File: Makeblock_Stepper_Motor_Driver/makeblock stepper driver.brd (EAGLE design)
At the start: 100 x 80 mm, 7 parts, among them IC1 A4988SETTR-T

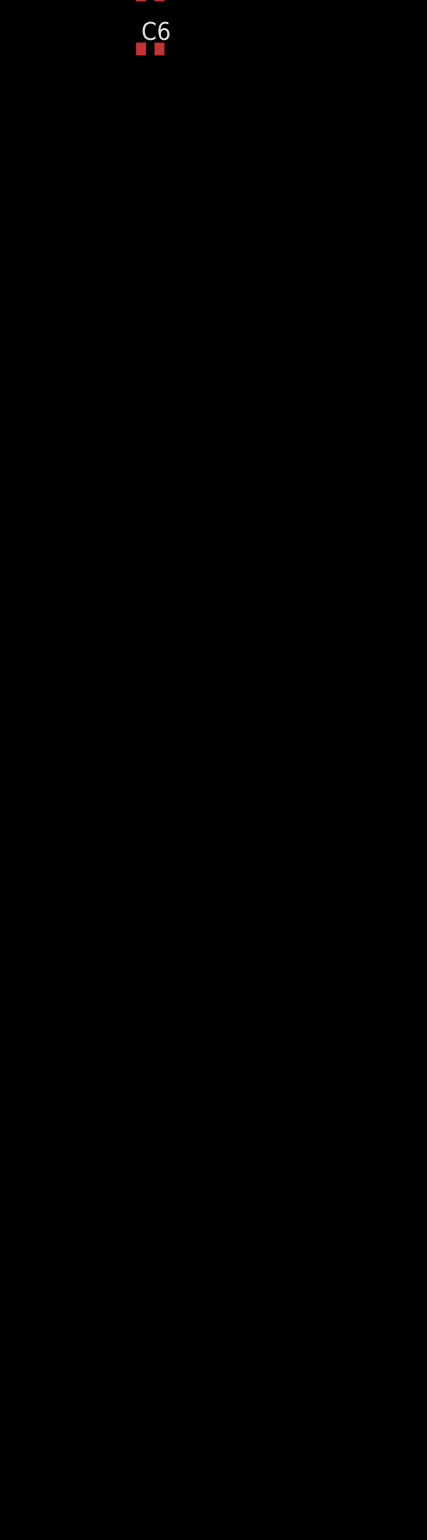
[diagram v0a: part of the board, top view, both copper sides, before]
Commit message: Added parts to the schematic
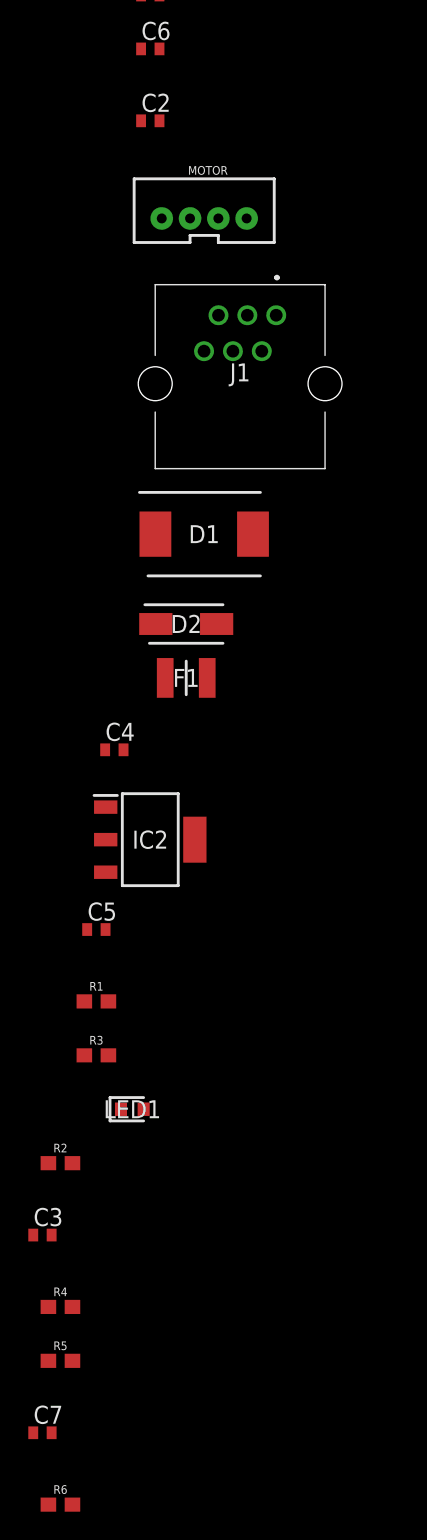
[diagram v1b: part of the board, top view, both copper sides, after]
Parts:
- added C2, C3, C4, C5, C7: 0.1uF, resistor:C0402
- added D1: SS34, SamacSys_Parts:DIOM8059X256N
- added D2: SS14, SamacSys_Parts:DIOM5227X270N
- added F1: 0ZCH0075AF2E, SamacSys_Parts:FUSC3226X75N
- added IC2: LD1117ASTR, SamacSys_Parts:SOT230P700X180-4N
- added J1: E5566-Q0LK22-L, SamacSys_Parts:E5566Q0LK22L
- added LED1: SML-D12U1WT86, SamacSys_Parts:LEDC1608X65N
- added MOTOR: (no value), SparkFun-Connectors:JST-4-PTH-VERT
- added R1, R4, R5, R6: 10M, SparkFun-Resistors:0603
- added R2: 100k, SparkFun-Resistors:0603
- added R3: 2.2k, SparkFun-Resistors:0603
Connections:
- removed net VCC: RN1.1, S1.1, S1.2, S1.3
- new net 1A: IC1.24, MOTOR.3
- new net 1B: IC1.21, MOTOR.4
- new net 2A: IC1.26, MOTOR.2
- new net 2B: IC1.1, MOTOR.1
- new net DIR: J1.5
- new net N$10: LED1.2, R3.1
- new net N$11: C5.2, IC2.2, IC2.4, R3.2
- new net N$12: IC1.2, R2.2
- new net N$13: C3.2, IC1.6
- new net N$14: IC1.27, R4.1
- new net N$15: IC1.23, R5.1
- new net N$16: IC1.19
- new net N$3: J1.1
- new net N$4: C2.2, IC1.28
- new net N$5: D1.1, F1.1
- new net N$6: C4.2, IC2.3
- new net N$9: J1.2
- new net PGND: C2.1, C7.1, IC1.18, IC1.29, IC1.3, R1.1, R5.2
- new net STEP: J1.6
- new net V-M: D1.2, D2.2, J1.3
- new net VM: C3.1, C7.2, F1.2, IC1.22
- net 5V: now also R6.2, RN1.1, S1.1, S1.2, S1.3
- net GND: now also C4.1, C5.1, D2.1, IC2.1, J1.4, LED1.1, R1.2, R2.1

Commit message: Finshed the schematic and the layout
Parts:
- added C10: 0.1u, resistor:C0402
- added P2: (no value), SparkFun-Connectors:1X04
- added P3: (no value), SparkFun-Connectors:1X03_LOCK
- added R7: 0.2R, SparkFun-Resistors:0603
- C1: value (none) -> 0.1uF
- C3: value 0.1uF -> 22uF; device resistor:C0402 -> rcl:C025-024X044
- R1: value 10M -> 0.2R
- R2: value 100k -> 0.2R
- R4: value 10M -> 27k
- R5: value 10M -> 100k
- R6: value 10M -> PVG3A203C01R00; device SparkFun-Resistors:0603 -> SamacSys_Parts:PVG3A203C01R00
- moved R6 148.2 mm to (13.0, 19.8)
- moved C7 138.6 mm to (19.9, 11.4)
- moved R5 130.7 mm to (19.7, 8.48)
- moved R4 123.7 mm to (2.71, 11.3)
- moved C3 118.2 mm to (20.5, 2.50)
- moved R2 111.5 mm to (8.21, 6.51)
- moved R3 110.8 mm to (25.2, 6.10)
- moved LED1 109.5 mm to (25.3, 2.29)
- moved R1 102.8 mm to (15.2, 6.32)
- moved C5 99.7 mm to (2.75, 13.5)
- moved IC2 99.6 mm to (5.08, 20.3)
- moved D1 91.5 mm to (24.6, 25.4), turned to 90 degrees
- moved J1 91.3 mm to (11.5, 44.5), turned to 180 degrees
- moved D2 90.2 mm to (25.4, 16.1), turned to 90 degrees
- moved C4 88.9 mm to (2.54, 15.2), turned to 180 degrees
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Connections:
- removed net N$12: IC1.2, R2.2
- removed net N$4: C2.2, IC1.28
- removed net ROSC: IC1.13, RN1.2
- new net EN: IC1.2, P3.1, R5.2
- new net N$17: IC1.17, R6.2
- net !RESET: now also C10.1, P3.2; no longer C1.1
- net !SLEEP: now also P3.3
- net 5V: now also R4.2; no longer R6.2
- net DIR: now also IC1.19, P2.2
- net GND: now also C10.2, P2.3, R5.1, R6.3, R7.2, RN1.2; no longer C1.2, C9.1, D2.1, R1.2, R2.1, RN1.7
- net N$13: now also C7.2; no longer C3.2
- net N$14: now also R1.1; no longer R4.1
- net N$15: now also R2.1; no longer R5.1
- net N$16: now also R4.1, R6.1; no longer IC1.19
- net N$6: now also D2.1
- net N$8: now also IC1.13, RN1.7; no longer IC1.16, RN1.5
- net PGND: now also C1.1, C3.2, C9.1, R2.2, R7.1; no longer C7.1, R1.1, R5.2
- net STEP: now also IC1.16, P2.1, RN1.5
- net V-M: now also P2.4
- net VM: now also C1.2, C2.2, C7.1, IC1.28; no longer C7.2
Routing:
- net GND: track 0.00 -> 147.1 mm, vias 0 -> 6
- net !SLEEP: track 0.00 -> 92.3 mm, vias 0 -> 5
- net N$11: track 0.00 -> 86.7 mm, vias 0 -> 4
- net !RESET: track 0.00 -> 77.0 mm, vias 0 -> 2
- net VM: track 0.00 -> 72.7 mm, vias 0 -> 6
- net V-M: track 0.00 -> 69.9 mm
- net STEP: track 0.00 -> 69.1 mm, vias 0 -> 4
- net PGND: track 0.00 -> 52.2 mm, vias 0 -> 4
- net MS3: track 0.00 -> 49.9 mm, vias 0 -> 2
- net 5V: track 0.00 -> 49.8 mm, vias 0 -> 8
- net N$14: track 0.00 -> 46.8 mm, vias 0 -> 4
- net DIR: track 0.00 -> 44.0 mm, vias 0 -> 2
- net N$15: track 0.00 -> 41.9 mm, vias 0 -> 2
- net N$6: track 0.00 -> 39.9 mm
- net EN: track 0.00 -> 38.2 mm, vias 0 -> 2
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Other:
- board size 100 x 80 mm -> 28.9 x 47.5 mm
